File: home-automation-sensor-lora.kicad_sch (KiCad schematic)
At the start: 95 parts, among them J1 Thermistor, J2 Conn_01x08, J3 Stemma-QT-Connector, J4 USB4105-GF-A_Lizard, J5 3V3-16V, J6 Conn_01x04, Q1 DMN2046U-7, Q2 DMN2046U-7, Q3 DMG3415U-7, U1 LD2985BM33R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

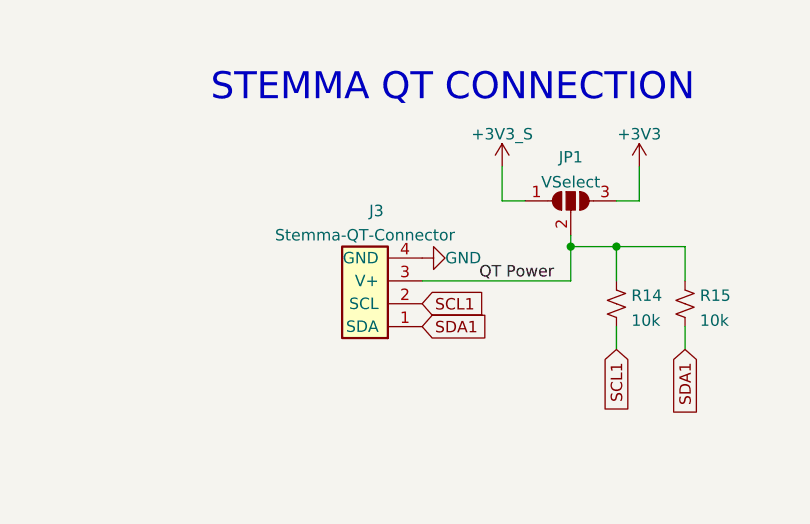
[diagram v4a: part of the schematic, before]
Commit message: corrected mirrored stemma qt connector pinout
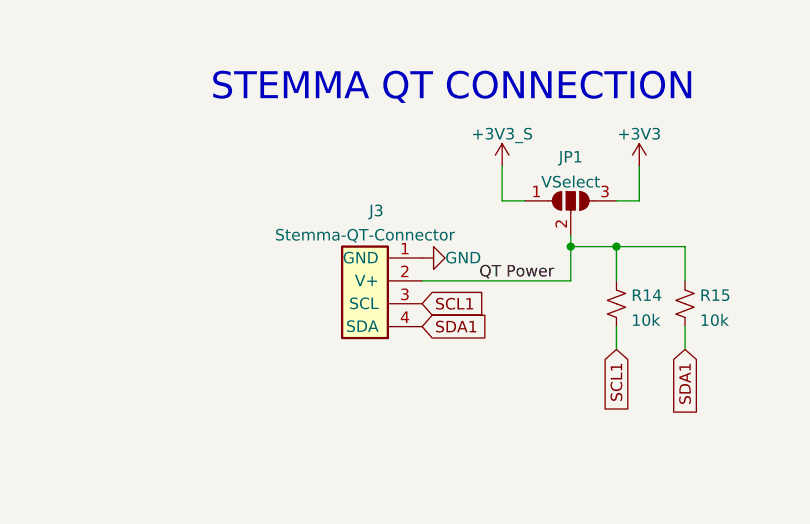
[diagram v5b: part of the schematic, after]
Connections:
- net GND: now also J3.1 (GND); no longer J3.4 (GND)
- net QT Power: now also J3.2 (V+); no longer J3.3 (V+)
- net SCL1: now also J3.3 (SCL); no longer J3.2 (SCL)
- net SDA1: now also J3.4 (SDA); no longer J3.1 (SDA)

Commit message: updated resistor values
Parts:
- R1, R10: value 1k -> 2k7
- R12: value 2.7k -> 2k7
- R14, R15: value 10k -> 2k7
- R5, R6, R7: value 5.1k -> 5k1
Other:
- moved on the sheet: R1, R15, R2
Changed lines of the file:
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@@
   (junction (at 31.75 161.29) (diameter 0) (color 0 0 0 0)
   )
-  (junction (at 252.73 101.6) (diameter 0) (color 0 0 0 0)
+  (junction (at 265.43 101.6) (diameter 0) (color 0 0 0 0)
   )
   (junction (at 298.45 49.53) (diameter 0) (color 0 0 0 0)
   )
+  (junction (at 251.46 163.83) (diameter 0) (color 0 0 0 0)
+  )
   (junction (at 40.64 105.41) (diameter 0) (color 0 0 0 0)
   )
@@
   (junction (at 219.71 247.65) (diameter 0) (color 0 0 0 0)
   )
-  (junction (at 252.73 163.83) (diameter 0) (color 0 0 0 0)
-  )
   (junction (at 160.02 181.61) (diameter 0) (color 0 0 0 0)
   )
@@
     (stroke (width 0) (type default))
   )
+  (wire (pts (xy 251.46 163.83) (xy 259.08 163.83))
+    (stroke (width 0) (type default))
+  )
   (wire (pts (xy 378.46 194.31) (xy 387.35 194.31))
     (stroke (width 0) (type default))
@@
     (stroke (width 0) (type default))
   )
-  (wire (pts (xy 245.11 163.83) (xy 252.73 163.83))
+  (wire (pts (xy 245.11 163.83) (xy 251.46 163.83))
     (stroke (width 0) (type default))
   )
@@
     (stroke (width 0) (type default))
   )
-  (wire (pts (xy 171.45 245.11) (xy 171.45 247.65))
+  (wire (pts (xy 172.72 245.11) (xy 172.72 247.65))
     (stroke (width 0) (type default))
   )
@@
     (stroke (width 0) (type default))
   )
-  (wire (pts (xy 245.11 101.6) (xy 252.73 101.6))
-    (stroke (width 0) (type default))
-  )
   (wire (pts (xy 219.71 149.86) (xy 219.71 154.94))
     (stroke (width 0) (type default))
@@
     (stroke (width 0) (type default))
   )
-  (wire (pts (xy 252.73 158.75) (xy 252.73 163.83))
+  (wire (pts (xy 251.46 158.75) (xy 251.46 163.83))
     (stroke (width 0) (type default))
   )
-  (wire (pts (xy 252.73 101.6) (xy 274.32 101.6))
+  (wire (pts (xy 245.11 101.6) (xy 265.43 101.6))
     (stroke (width 0) (type default))
   )
@@
     (stroke (width 0) (type default))
   )
-  (wire (pts (xy 252.73 163.83) (xy 259.08 163.83))
-    (stroke (width 0) (type default))
-  )
   (wire (pts (xy 382.27 50.8) (xy 391.16 50.8))
     (stroke (width 0) (type default))
@@
     (stroke (width 0) (type default))
   )
-  (wire (pts (xy 171.45 240.03) (xy 171.45 236.22))
+  (wire (pts (xy 172.72 240.03) (xy 172.72 236.22))
     (stroke (width 0) (type default))
   )
@@
     (stroke (width 0) (type default))
   )
+  (wire (pts (xy 265.43 101.6) (xy 274.32 101.6))
+    (stroke (width 0) (type default))
+  )
   (wire (pts (xy 40.64 105.41) (xy 48.26 105.41))
     (stroke (width 0) (type default))
@@
     (stroke (width 0) (type default))
   )
-  (wire (pts (xy 171.45 236.22) (xy 163.83 236.22))
+  (wire (pts (xy 163.83 236.22) (xy 172.72 236.22))
     (stroke (width 0) (type default))
   )
@@
     (stroke (width 0) (type default))
   )
-  (wire (pts (xy 252.73 87.63) (xy 252.73 91.44))
+  (wire (pts (xy 265.43 87.63) (xy 265.43 91.44))
     (stroke (width 0) (type default))
   )
@@
     (stroke (width 0) (type default))
   )
-  (wire (pts (xy 252.73 96.52) (xy 252.73 101.6))
+  (wire (pts (xy 265.43 96.52) (xy 265.43 101.6))
     (stroke (width 0) (type default))
   )
@@
     (stroke (width 0) (type default))
   )
-  (wire (pts (xy 252.73 149.86) (xy 252.73 153.67))
+  (wire (pts (xy 251.46 149.86) (xy 251.46 153.67))
     (stroke (width 0) (type default))
   )
@@
     )
   )
-  (global_label "SDA1" (shape input) (at 171.45 247.65 270) (fields_autoplaced)
+  (global_label "SDA1" (shape input) (at 172.72 247.65 270) (fields_autoplaced)
     (effects (font (size 1.27 1.27)) (justify right))
-    (property "Intersheetrefs" "${INTERSHEET_REFS}" (at 171.5294 254.8407 90)
+    (property "Intersheetrefs" "${INTERSHEET_REFS}" (at 172.7994 254.8407 90)
       (effects (font (size 1.27 1.27)) (justify right) hide)
     )
@@
       (effects (font (size 1.27 1.27)) (justify left))
     )
-    (property "Value" "2.7k" (at 96.52 48.26 0)
+    (property "Value" "2k7" (at 96.52 48.26 0)
       (effects (font (size 1.27 1.27)) (justify left))
     )
@@
     )
   )
-  (symbol (lib_id "power:+3V3") (at 252.73 87.63 0) (unit 1)
+  (symbol (lib_id "power:+3V3") (at 265.43 87.63 0) (unit 1)
     (in_bom yes) (on_board yes) (dnp no) (fields_autoplaced)
-    (property "Reference" "#PWR0112" (at 252.73 91.44 0)
+    (property "Reference" "#PWR0112" (at 265.43 91.44 0)
       (effects (font (size 1.27 1.27)) hide)
     )
-    (property "Value" "+3V3" (at 252.73 84.0255 0)
+    (property "Value" "+3V3" (at 265.43 84.0255 0)
       (effects (font (size 1.27 1.27)))
     )
-    (property "Footprint" "" (at 252.73 87.63 0)
+    (property "Footprint" "" (at 265.43 87.63 0)
       (effects (font (size 1.27 1.27)) hide)
     )
-    (property "Datasheet" "" (at 252.73 87.63 0)
+    (property "Datasheet" "" (at 265.43 87.63 0)
       (effects (font (size 1.27 1.27)) hide)
     )
@@
   (symbol (lib_id "Device:R_Small_US") (at 245.11 93.98 0) (unit 1)
     (in_bom yes) (on_board yes) (dnp no) (fields_autoplaced)
-    (property "Reference" "R10" (at 246.761 93.0715 0)
+    (property "Reference" "R10" (at 247.65 93.345 0)
       (effects (font (size 1.27 1.27)) (justify left))
     )
-    (property "Value" "1k" (at 246.761 95.8466 0)
+    (property "Value" "2k7" (at 247.65 95.885 0)
       (effects (font (size 1.27 1.27)) (justify left))
     )
@@
     )
   )
-  (symbol (lib_id "Device:R_Small_US") (at 252.73 93.98 0) (unit 1)
+  (symbol (lib_id "Device:R_Small_US") (at 265.43 93.98 0) (unit 1)
     (in_bom yes) (on_board yes) (dnp no) (fields_autoplaced)
-    (property "Reference" "R2" (at 254.381 93.0715 0)
+    (property "Reference" "R2" (at 267.081 93.0715 0)
       (effects (font (size 1.27 1.27)) (justify left))
     )
-    (property "Value" "DNF" (at 254.381 95.8466 0)
+    (property "Value" "DNF" (at 267.081 95.8466 0)
       (effects (font (size 1.27 1.27)) (justify left))
     )
-    (property "Footprint" "lizard_libs:R_0603_Lizard" (at 252.73 93.98 0)
+    (property "Footprint" "lizard_libs:R_0603_Lizard" (at 265.43 93.98 0)
       (effects (font (size 1.27 1.27)) hide)
     )
-    (property "Datasheet" "~" (at 252.73 93.98 0)
+    (property "Datasheet" "~" (at 265.43 93.98 0)
       (effects (font (size 1.27 1.27)) hide)
     )
@@
   (symbol (lib_id "Device:R_Small_US") (at 163.83 242.57 0) (unit 1)
     (in_bom yes) (on_board yes) (dnp no) (fields_autoplaced)
-    (property "Reference" "R14" (at 165.481 241.6615 0)
+    (property "Reference" "R14" (at 166.37 241.935 0)
       (effects (font (size 1.27 1.27)) (justify left))
     )
-    (property "Value" "10k" (at 165.481 244.4366 0)
+    (property "Value" "2k7" (at 166.37 244.475 0)
       (effects (font (size 1.27 1.27)) (justify left))
     )
@@
       (effects (font (size 1.27 1.27)) (justify left))
     )
-    (property "Value" "5.1k" (at 81.28 231.14 0)
+    (property "Value" "5k1" (at 81.28 231.14 0)
       (effects (font (size 1.27 1.27)) (justify left))
     )
@@
       (effects (font (size 1.27 1.27)) (justify left))
     )
-    (property "Value" "5.1k" (at 97.79 179.07 0)
+    (property "Value" "5k1" (at 97.79 179.07 0)
       (effects (font (size 1.27 1.27)) (justify left))
     )
@@
     )
   )
-  (symbol (lib_id "Device:R_Small_US") (at 252.73 156.21 0) (unit 1)
+  (symbol (lib_id "Device:R_Small_US") (at 251.46 156.21 0) (unit 1)
     (in_bom yes) (on_board yes) (dnp no) (fields_autoplaced)
-    (property "Reference" "R1" (at 255.27 154.9399 0)
+    (property "Reference" "R1" (at 254 155.575 0)
       (effects (font (size 1.27 1.27)) (justify left))
     )
-    (property "Value" "1k" (at 255.27 157.4799 0)
+    (property "Value" "2k7" (at 254 158.115 0)
       (effects (font (size 1.27 1.27)) (justify left))
     )
-    (property "Footprint" "lizard_libs:R_0603_Lizard" (at 252.73 156.21 0)
+    (property "Footprint" "lizard_libs:R_0603_Lizard" (at 251.46 156.21 0)
       (effects (font (size 1.27 1.27)) hide)
     )
-    (property "Datasheet" "~" (at 252.73 156.21 0)
+    (property "Datasheet" "~" (at 251.46 156.21 0)
       (effects (font (size 1.27 1.27)) hide)
     )
@@
     )
   )
-  (symbol (lib_id "Device:R_Small_US") (at 171.45 242.57 0) (unit 1)
+  (symbol (lib_id "Device:R_Small_US") (at 172.72 242.57 0) (unit 1)
     (in_bom yes) (on_board yes) (dnp no) (fields_autoplaced)
-    (property "Reference" "R15" (at 173.101 241.6615 0)
+    (property "Reference" "R15" (at 175.26 241.935 0)
       (effects (font (size 1.27 1.27)) (justify left))
     )
-    (property "Value" "10k" (at 173.101 244.4366 0)
+    (property "Value" "2k7" (at 175.26 244.475 0)
       (effects (font (size 1.27 1.27)) (justify left))
     )
-    (property "Footprint" "lizard_libs:R_0603_Lizard" (at 171.45 242.57 0)
+    (property "Footprint" "lizard_libs:R_0603_Lizard" (at 172.72 242.57 0)
       (effects (font (size 1.27 1.27)) hide)
     )
-    (property "Datasheet" "~" (at 171.45 242.57 0)
+    (property "Datasheet" "~" (at 172.72 242.57 0)
       (effects (font (size 1.27 1.27)) hide)
     )
@@
       (effects (font (size 1.27 1.27)) (justify left))
     )
-    (property "Value" "5.1k" (at 88.9 228.6 0)
+    (property "Value" "5k1" (at 88.9 228.6 0)
       (effects (font (size 1.27 1.27)) (justify left))
     )
@@
     )
   )
-  (symbol (lib_id "power:+3V3") (at 252.73 149.86 0) (unit 1)
+  (symbol (lib_id "power:+3V3") (at 251.46 149.86 0) (unit 1)
     (in_bom yes) (on_board yes) (dnp no) (fields_autoplaced)
-    (property "Reference" "#PWR036" (at 252.73 153.67 0)
+    (property "Reference" "#PWR036" (at 251.46 153.67 0)
       (effects (font (size 1.27 1.27)) hide)
     )
-    (property "Value" "+3V3" (at 252.73 146.2555 0)
+    (property "Value" "+3V3" (at 251.46 146.2555 0)
       (effects (font (size 1.27 1.27)))
     )
-    (property "Footprint" "" (at 252.73 149.86 0)
+    (property "Footprint" "" (at 251.46 149.86 0)
       (effects (font (size 1.27 1.27)) hide)
     )
-    (property "Datasheet" "" (at 252.73 149.86 0)
+    (property "Datasheet" "" (at 251.46 149.86 0)
       (effects (font (size 1.27 1.27)) hide)
     )

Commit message: updated BMS to auto-start version
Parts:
- U7: value AP9101CK6-ANTRG1 -> AP9101CAK6-ANTRG1; symbol lizard_lib:AP9101CK6-ANTRG1 -> lizard_lib:AP9101CAK6-ANTRG1
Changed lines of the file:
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@@
     )
   )
-  (symbol (lib_id "lizard_lib:AP9101CK6-ANTRG1") (at 68.58 39.37 0) (unit 1)
-    (in_bom yes) (on_board yes) (dnp no) (fields_autoplaced)
+  (symbol (lib_id "lizard_lib:AP9101CAK6-ANTRG1") (at 68.58 39.37 0) (unit 1)
+    (in_bom yes) (on_board yes) (dnp no)
     (property "Reference" "U7" (at 68.58 30.48 0)
       (effects (font (size 1.27 1.27)))
     )
-    (property "Value" "AP9101CK6-ANTRG1" (at 68.58 33.02 0)
+    (property "Value" "AP9101CAK6-ANTRG1" (at 68.58 33.02 0)
       (effects (font (size 1.27 1.27)))
     )
